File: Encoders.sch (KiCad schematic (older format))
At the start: 32 parts

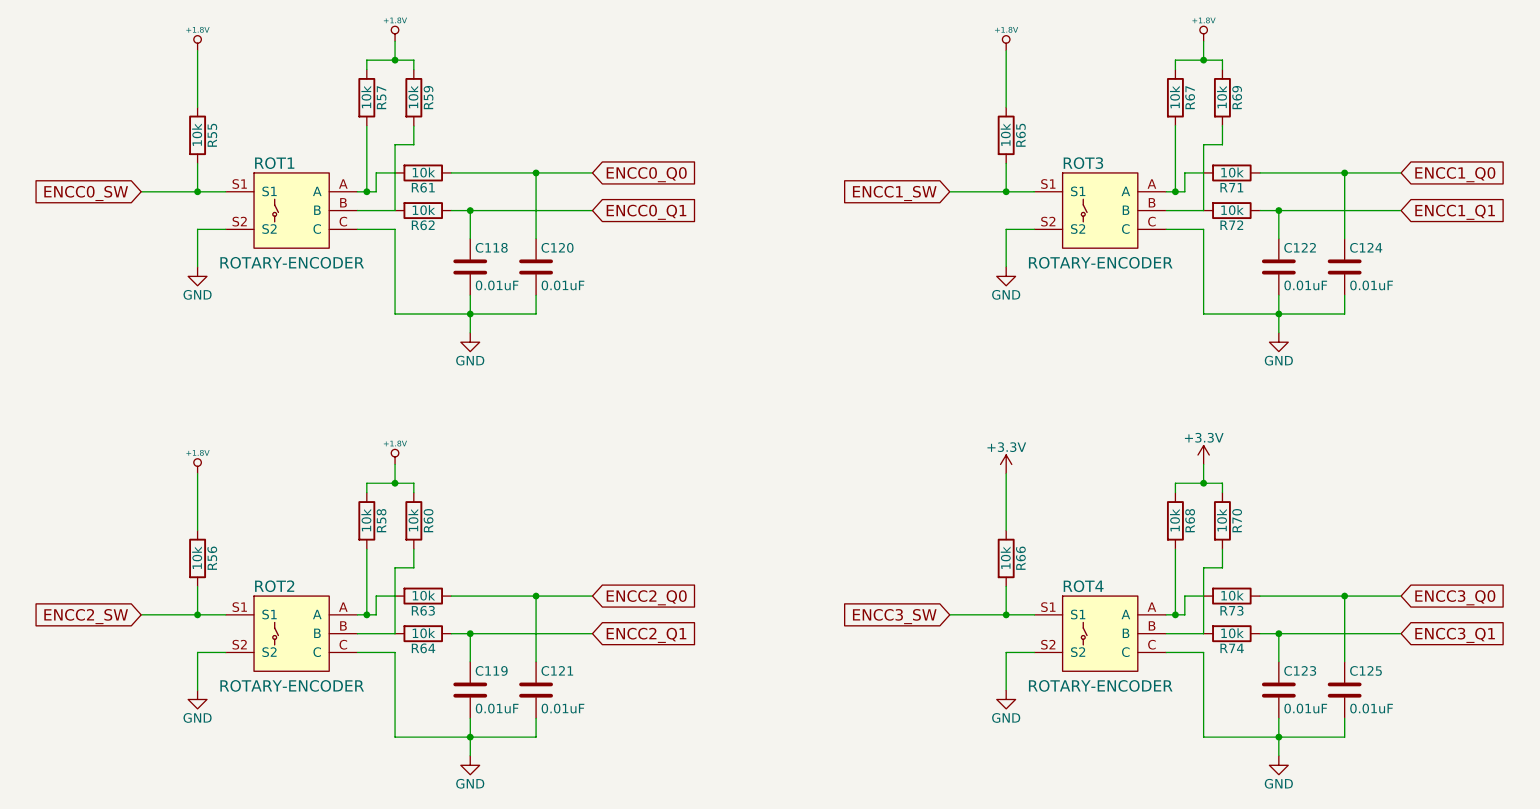
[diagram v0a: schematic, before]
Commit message: fixed all schematic/footprint errors
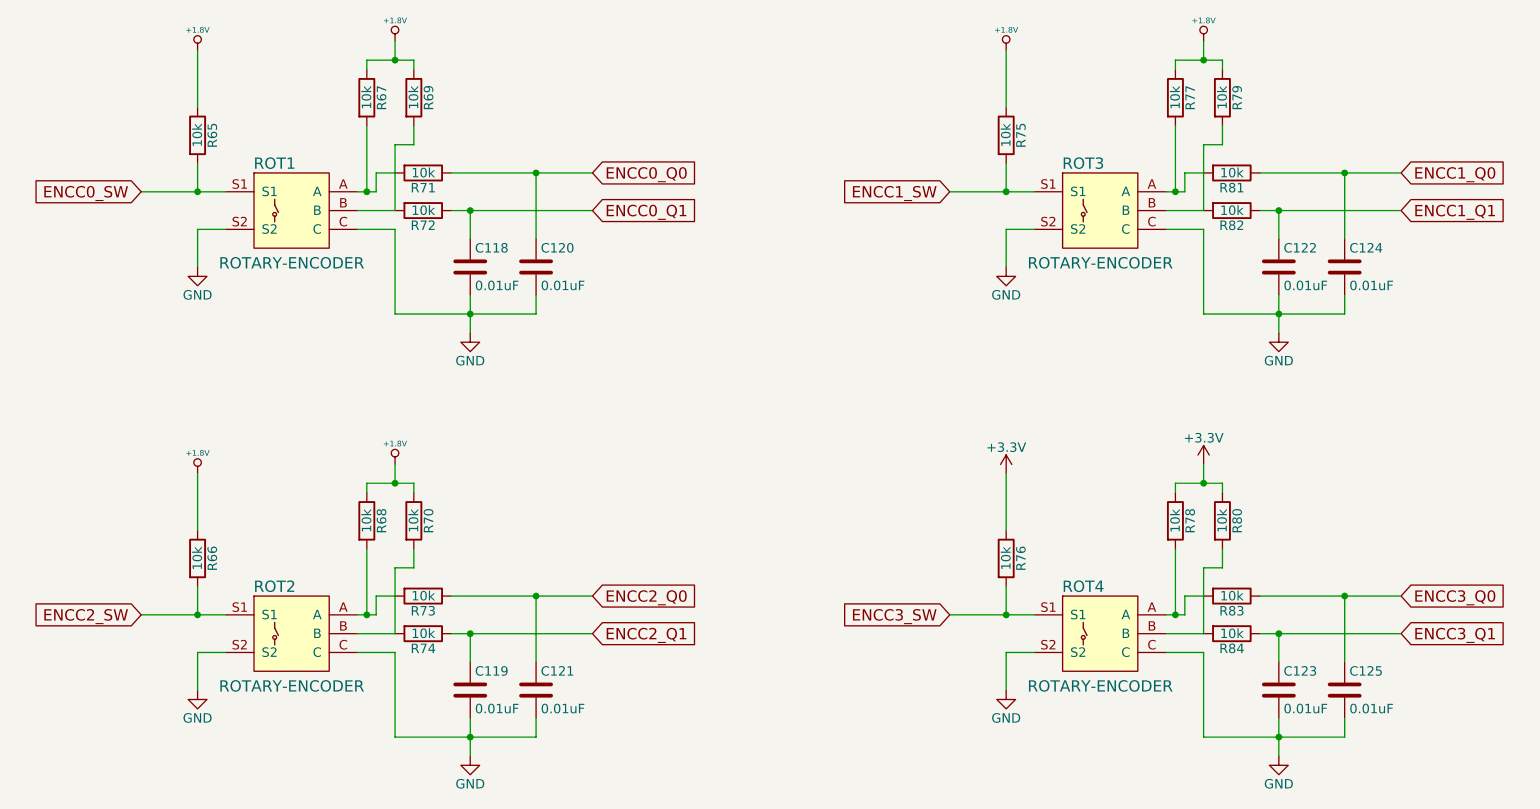
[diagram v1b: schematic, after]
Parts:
- renumbered R55 to R65, R56 to R66, R57 to R67, R58 to R68, R59 to R69, R60 to R70, R61 to R71, R62 to R72, R63 to R73, R64 to R74, R65 to R75, R66 to R76, R67 to R77, R68 to R78, R69 to R79, R70 to R80, R71 to R81, R72 to R82, R73 to R83, R74 to R84
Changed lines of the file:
@@
 $EndComp
 $Comp
-L R R62
+L R R72
 U 1 1 586C395E
 P 4150 2600
-F 0 "R62" V 4230 2600 50  0000 C CNN
+F 0 "R72" V 4230 2600 50  0000 C CNN
 F 1 "10k" V 4150 2600 50  0000 C CNN
 F 2 "Resistors_SMD:R_1206" V 4080 2600 50  0001 C CNN
@@
 $EndComp
 $Comp
-L R R61
+L R R71
 U 1 1 586C39C5
 P 4150 2400
-F 0 "R61" V 4230 2400 50  0000 C CNN
+F 0 "R71" V 4230 2400 50  0000 C CNN
 F 1 "10k" V 4150 2400 50  0000 C CNN
 F 2 "Resistors_SMD:R_1206" V 4080 2400 50  0001 C CNN
@@
 	4750 2400 4750 2750
 $Comp
-L R R57
+L R R67
 U 1 1 586C3A50
 P 3850 2000
-F 0 "R57" V 3930 2000 50  0000 C CNN
+F 0 "R67" V 3930 2000 50  0000 C CNN
 F 1 "10k" V 3850 2000 50  0000 C CNN
 F 2 "Resistors_SMD:R_1206" V 3780 2000 50  0001 C CNN
@@
 $EndComp
 $Comp
-L R R59
+L R R69
 U 1 1 586C3A87
 P 4100 2000
-F 0 "R59" V 4180 2000 50  0000 C CNN
+F 0 "R69" V 4180 2000 50  0000 C CNN
 F 1 "10k" V 4100 2000 50  0000 C CNN
 F 2 "Resistors_SMD:R_1206" V 4030 2000 50  0001 C CNN
@@
 Connection ~ 4000 1800
 $Comp
-L +1.8V #PWR0136
+L +1.8V #PWR0138
 U 1 1 586C41F4
 P 4000 1700
-F 0 "#PWR0136" H 4000 1840 20  0001 C CNN
+F 0 "#PWR0138" H 4000 1840 20  0001 C CNN
 F 1 "+1.8V" H 4000 1810 30  0000 C CNN
 F 2 "" H 4000 1700 60  0001 C CNN
@@
 $EndComp
 $Comp
-L GND #PWR0137
+L GND #PWR0139
 U 1 1 586C4216
 P 4400 3250
-F 0 "#PWR0137" H 4400 3000 50  0001 C CNN
+F 0 "#PWR0139" H 4400 3000 50  0001 C CNN
 F 1 "GND" H 4400 3100 50  0000 C CNN
 F 2 "" H 4400 3250 50  0000 C CNN
@@
 $EndComp
 $Comp
-L R R55
+L R R65
 U 1 1 586C42C6
 P 2950 2200
-F 0 "R55" V 3030 2200 50  0000 C CNN
+F 0 "R65" V 3030 2200 50  0000 C CNN
 F 1 "10k" V 2950 2200 50  0000 C CNN
 F 2 "Resistors_SMD:R_1206" V 2880 2200 50  0001 C CNN
@@
 	2950 2700 2950 2900
 $Comp
-L GND #PWR0138
+L GND #PWR0140
 U 1 1 586C437C
 P 2950 2900
-F 0 "#PWR0138" H 2950 2650 50  0001 C CNN
+F 0 "#PWR0140" H 2950 2650 50  0001 C CNN
 F 1 "GND" H 2950 2750 50  0000 C CNN
 F 2 "" H 2950 2900 50  0000 C CNN
@@
 $EndComp
 $Comp
-L +1.8V #PWR0139
+L +1.8V #PWR0141
 U 1 1 586C43A0
 P 2950 1750
-F 0 "#PWR0139" H 2950 1890 20  0001 C CNN
+F 0 "#PWR0141" H 2950 1890 20  0001 C CNN
 F 1 "+1.8V" H 2950 1860 30  0000 C CNN
 F 2 "" H 2950 1750 60  0001 C CNN
@@
 $EndComp
 $Comp
-L R R72
+L R R82
 U 1 1 586C5704
 P 8450 2600
-F 0 "R72" V 8530 2600 50  0000 C CNN
+F 0 "R82" V 8530 2600 50  0000 C CNN
 F 1 "10k" V 8450 2600 50  0000 C CNN
 F 2 "Resistors_SMD:R_1206" V 8380 2600 50  0001 C CNN
@@
 $EndComp
 $Comp
-L R R71
+L R R81
 U 1 1 586C570A
 P 8450 2400
-F 0 "R71" V 8530 2400 50  0000 C CNN
+F 0 "R81" V 8530 2400 50  0000 C CNN
 F 1 "10k" V 8450 2400 50  0000 C CNN
 F 2 "Resistors_SMD:R_1206" V 8380 2400 50  0001 C CNN
@@
 	9050 2400 9050 2750
 $Comp
-L R R67
+L R R77
 U 1 1 586C5718
 P 8150 2000
-F 0 "R67" V 8230 2000 50  0000 C CNN
+F 0 "R77" V 8230 2000 50  0000 C CNN
 F 1 "10k" V 8150 2000 50  0000 C CNN
 F 2 "Resistors_SMD:R_1206" V 8080 2000 50  0001 C CNN
@@
 $EndComp
 $Comp
-L R R69
+L R R79
 U 1 1 586C571E
 P 8400 2000
-F 0 "R69" V 8480 2000 50  0000 C CNN
+F 0 "R79" V 8480 2000 50  0000 C CNN
 F 1 "10k" V 8400 2000 50  0000 C CNN
 F 2 "Resistors_SMD:R_1206" V 8330 2000 50  0001 C CNN
@@
 Connection ~ 8300 1800
 $Comp
-L +1.8V #PWR0140
+L +1.8V #PWR0142
 U 1 1 586C5734
 P 8300 1700
-F 0 "#PWR0140" H 8300 1840 20  0001 C CNN
+F 0 "#PWR0142" H 8300 1840 20  0001 C CNN
 F 1 "+1.8V" H 8300 1810 30  0000 C CNN
 F 2 "" H 8300 1700 60  0001 C CNN
@@
 $EndComp
 $Comp
-L GND #PWR0141
+L GND #PWR0143
 U 1 1 586C573A
 P 8700 3250
-F 0 "#PWR0141" H 8700 3000 50  0001 C CNN
+F 0 "#PWR0143" H 8700 3000 50  0001 C CNN
 F 1 "GND" H 8700 3100 50  0000 C CNN
 F 2 "" H 8700 3250 50  0000 C CNN
@@
 $EndComp
 $Comp
-L R R65
+L R R75
 U 1 1 586C5740
 P 7250 2200
-F 0 "R65" V 7330 2200 50  0000 C CNN
+F 0 "R75" V 7330 2200 50  0000 C CNN
 F 1 "10k" V 7250 2200 50  0000 C CNN
 F 2 "Resistors_SMD:R_1206" V 7180 2200 50  0001 C CNN
@@
 	7250 2700 7250 2900
 $Comp
-L GND #PWR0142
+L GND #PWR0144
 U 1 1 586C5748
 P 7250 2900
-F 0 "#PWR0142" H 7250 2650 50  0001 C CNN
+F 0 "#PWR0144" H 7250 2650 50  0001 C CNN
 F 1 "GND" H 7250 2750 50  0000 C CNN
 F 2 "" H 7250 2900 50  0000 C CNN
@@
 $EndComp
 $Comp
-L +1.8V #PWR0143
+L +1.8V #PWR0145
 U 1 1 586C574E
 P 7250 1750
-F 0 "#PWR0143" H 7250 1890 20  0001 C CNN
+F 0 "#PWR0145" H 7250 1890 20  0001 C CNN
 F 1 "+1.8V" H 7250 1860 30  0000 C CNN
 F 2 "" H 7250 1750 60  0001 C CNN
@@
 $EndComp
 $Comp
-L R R64
+L R R74
 U 1 1 586C5B4F
 P 4150 4850
-F 0 "R64" V 4230 4850 50  0000 C CNN
+F 0 "R74" V 4230 4850 50  0000 C CNN
 F 1 "10k" V 4150 4850 50  0000 C CNN
 F 2 "Resistors_SMD:R_1206" V 4080 4850 50  0001 C CNN
@@
 $EndComp
 $Comp
-L R R63
+L R R73
 U 1 1 586C5B55
 P 4150 4650
-F 0 "R63" V 4230 4650 50  0000 C CNN
+F 0 "R73" V 4230 4650 50  0000 C CNN
 F 1 "10k" V 4150 4650 50  0000 C CNN
 F 2 "Resistors_SMD:R_1206" V 4080 4650 50  0001 C CNN
@@
 	4750 4650 4750 5000
 $Comp
-L R R58
+L R R68
 U 1 1 586C5B63
 P 3850 4250
-F 0 "R58" V 3930 4250 50  0000 C CNN
+F 0 "R68" V 3930 4250 50  0000 C CNN
 F 1 "10k" V 3850 4250 50  0000 C CNN
 F 2 "Resistors_SMD:R_1206" V 3780 4250 50  0001 C CNN
@@
 $EndComp
 $Comp
-L R R60
+L R R70
 U 1 1 586C5B69
 P 4100 4250
-F 0 "R60" V 4180 4250 50  0000 C CNN
+F 0 "R70" V 4180 4250 50  0000 C CNN
 F 1 "10k" V 4100 4250 50  0000 C CNN
 F 2 "Resistors_SMD:R_1206" V 4030 4250 50  0001 C CNN
@@
 Connection ~ 4000 4050
 $Comp
-L +1.8V #PWR0144
+L +1.8V #PWR0146
 U 1 1 586C5B7F
 P 4000 3950
-F 0 "#PWR0144" H 4000 4090 20  0001 C CNN
+F 0 "#PWR0146" H 4000 4090 20  0001 C CNN
 F 1 "+1.8V" H 4000 4060 30  0000 C CNN
 F 2 "" H 4000 3950 60  0001 C CNN
@@
 $EndComp
 $Comp
-L GND #PWR0145
+L GND #PWR0147
 U 1 1 586C5B85
 P 4400 5500
-F 0 "#PWR0145" H 4400 5250 50  0001 C CNN
+F 0 "#PWR0147" H 4400 5250 50  0001 C CNN
 F 1 "GND" H 4400 5350 50  0000 C CNN
 F 2 "" H 4400 5500 50  0000 C CNN
@@
 $EndComp
 $Comp
-L R R56
+L R R66
 U 1 1 586C5B8B
 P 2950 4450
-F 0 "R56" V 3030 4450 50  0000 C CNN
+F 0 "R66" V 3030 4450 50  0000 C CNN
 F 1 "10k" V 2950 4450 50  0000 C CNN
 F 2 "Resistors_SMD:R_1206" V 2880 4450 50  0001 C CNN
@@
 	2950 4950 2950 5150
 $Comp
-L GND #PWR0146
+L GND #PWR0148
 U 1 1 586C5B93
 P 2950 5150
-F 0 "#PWR0146" H 2950 4900 50  0001 C CNN
+F 0 "#PWR0148" H 2950 4900 50  0001 C CNN
 F 1 "GND" H 2950 5000 50  0000 C CNN
 F 2 "" H 2950 5150 50  0000 C CNN
@@
 $EndComp
 $Comp
-L +1.8V #PWR0147
+L +1.8V #PWR0149
 U 1 1 586C5B99
 P 2950 4000
-F 0 "#PWR0147" H 2950 4140 20  0001 C CNN
+F 0 "#PWR0149" H 2950 4140 20  0001 C CNN
 F 1 "+1.8V" H 2950 4110 30  0000 C CNN
 F 2 "" H 2950 4000 60  0001 C CNN
@@
 $EndComp
 $Comp
-L R R74
+L R R84
 U 1 1 586C626A
 P 8450 4850
-F 0 "R74" V 8530 4850 50  0000 C CNN
+F 0 "R84" V 8530 4850 50  0000 C CNN
 F 1 "10k" V 8450 4850 50  0000 C CNN
 F 2 "Resistors_SMD:R_1206" V 8380 4850 50  0001 C CNN
@@
 $EndComp
 $Comp
-L R R73
+L R R83
 U 1 1 586C6270
 P 8450 4650
-F 0 "R73" V 8530 4650 50  0000 C CNN
+F 0 "R83" V 8530 4650 50  0000 C CNN
 F 1 "10k" V 8450 4650 50  0000 C CNN
 F 2 "Resistors_SMD:R_1206" V 8380 4650 50  0001 C CNN
@@
 	9050 4650 9050 5000
 $Comp
-L R R68
+L R R78
 U 1 1 586C627E
 P 8150 4250
-F 0 "R68" V 8230 4250 50  0000 C CNN
+F 0 "R78" V 8230 4250 50  0000 C CNN
 F 1 "10k" V 8150 4250 50  0000 C CNN
 F 2 "Resistors_SMD:R_1206" V 8080 4250 50  0001 C CNN
@@
 $EndComp
 $Comp
-L R R70
+L R R80
 U 1 1 586C6284
 P 8400 4250
-F 0 "R70" V 8480 4250 50  0000 C CNN
+F 0 "R80" V 8480 4250 50  0000 C CNN
 F 1 "10k" V 8400 4250 50  0000 C CNN
 F 2 "Resistors_SMD:R_1206" V 8330 4250 50  0001 C CNN
@@
 Connection ~ 8300 4050
 $Comp
-L GND #PWR0148
+L GND #PWR0150
 U 1 1 586C62A0
 P 8700 5500
-F 0 "#PWR0148" H 8700 5250 50  0001 C CNN
+F 0 "#PWR0150" H 8700 5250 50  0001 C CNN
 F 1 "GND" H 8700 5350 50  0000 C CNN
 F 2 "" H 8700 5500 50  0000 C CNN
@@
 $EndComp
 $Comp
-L R R66
+L R R76
 U 1 1 586C62A6
 P 7250 4450
-F 0 "R66" V 7330 4450 50  0000 C CNN
+F 0 "R76" V 7330 4450 50  0000 C CNN
 F 1 "10k" V 7250 4450 50  0000 C CNN
 F 2 "Resistors_SMD:R_1206" V 7180 4450 50  0001 C CNN
@@
 	7250 4950 7250 5150
 $Comp
-L GND #PWR0149
+L GND #PWR0151
 U 1 1 586C62AE
 P 7250 5150
-F 0 "#PWR0149" H 7250 4900 50  0001 C CNN
+F 0 "#PWR0151" H 7250 4900 50  0001 C CNN
 F 1 "GND" H 7250 5000 50  0000 C CNN
 F 2 "" H 7250 5150 50  0000 C CNN
@@
 Connection ~ 7250 4750
 $Comp
-L +3.3V #PWR0150
+L +3.3V #PWR0152
 U 1 1 587428B8
 P 8300 3950
-F 0 "#PWR0150" H 8300 3800 50  0001 C CNN
+F 0 "#PWR0152" H 8300 3800 50  0001 C CNN
 F 1 "+3.3V" H 8300 4090 50  0000 C CNN
 F 2 "" H 8300 3950 50  0000 C CNN
@@
 $EndComp
 $Comp
-L +3.3V #PWR0151
+L +3.3V #PWR0153
 U 1 1 58742FBB
 P 7250 4000
-F 0 "#PWR0151" H 7250 3850 50  0001 C CNN
+F 0 "#PWR0153" H 7250 3850 50  0001 C CNN
 F 1 "+3.3V" H 7250 4140 50  0000 C CNN
 F 2 "" H 7250 4000 50  0000 C CNN
